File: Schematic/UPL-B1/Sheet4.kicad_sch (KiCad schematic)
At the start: 60 parts

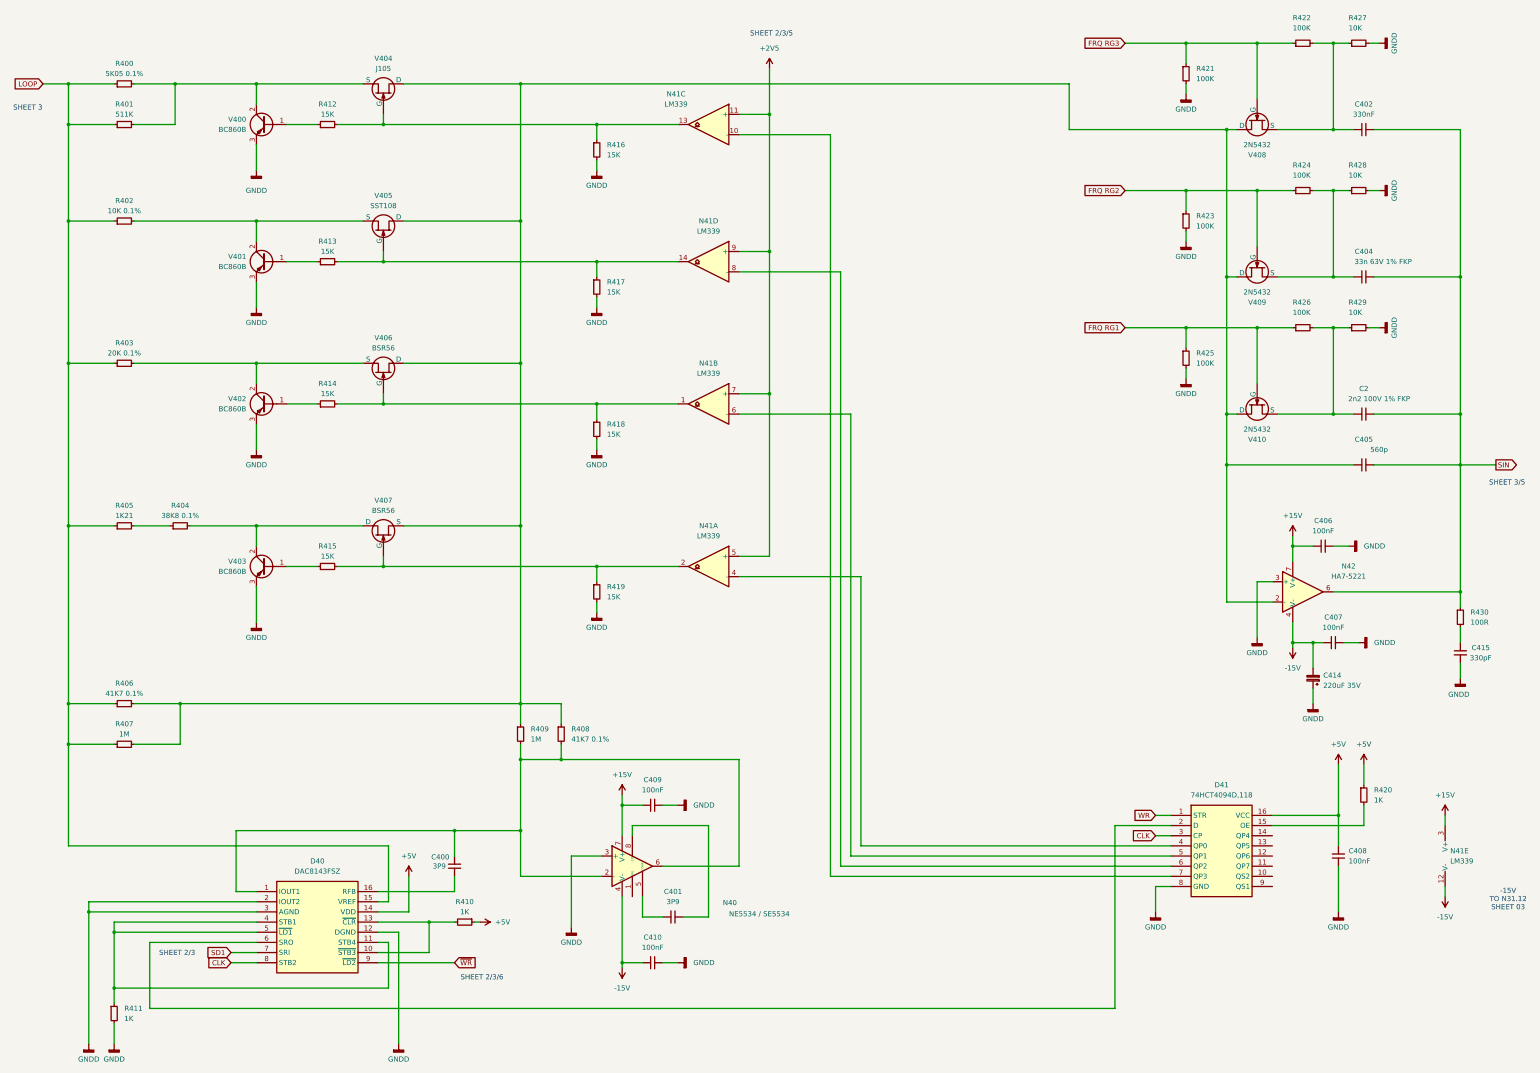
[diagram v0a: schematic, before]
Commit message: Added Integrator 1 and Level control
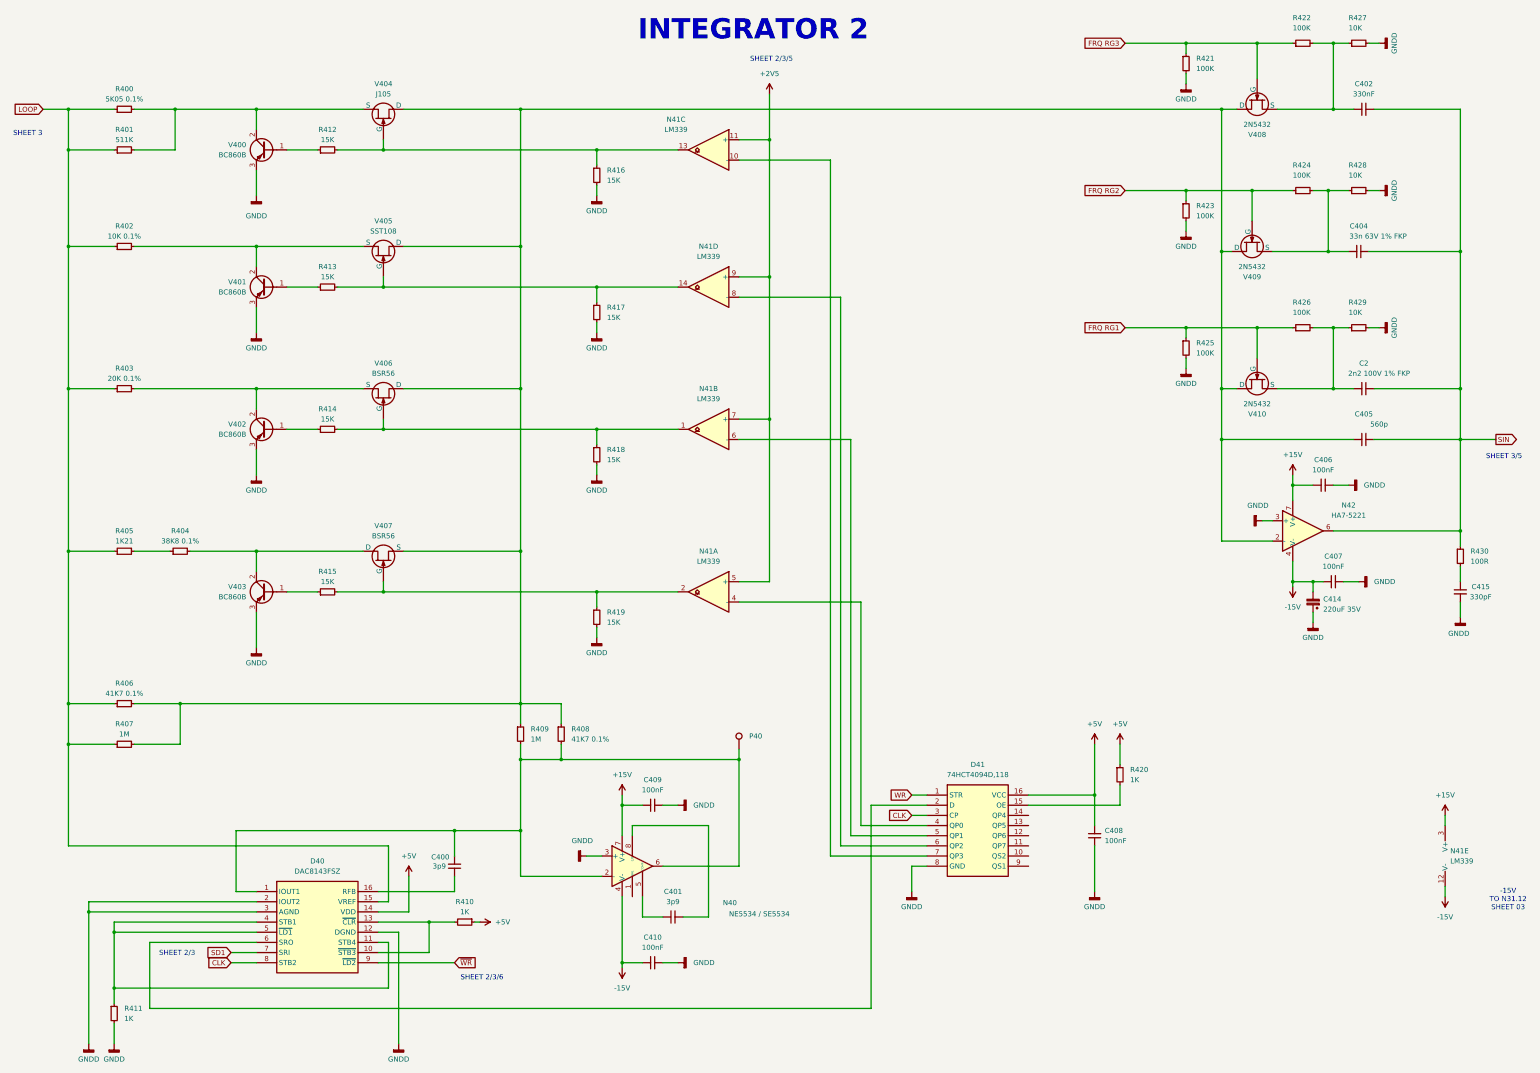
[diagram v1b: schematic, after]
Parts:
- added P40: TestPoint, symbol Connector:TestPoint
- C400, C401: value 3P9 -> 3p9
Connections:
- net at C400.2, D40.1 (IOUT1), N40.2 (-)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: now also P40.1
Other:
- note added: "INTEGRATOR 2"
- moved on the sheet: C2, C402, C404, C405, C406, C407, C408, C414, C415, D41, N41A, N41B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

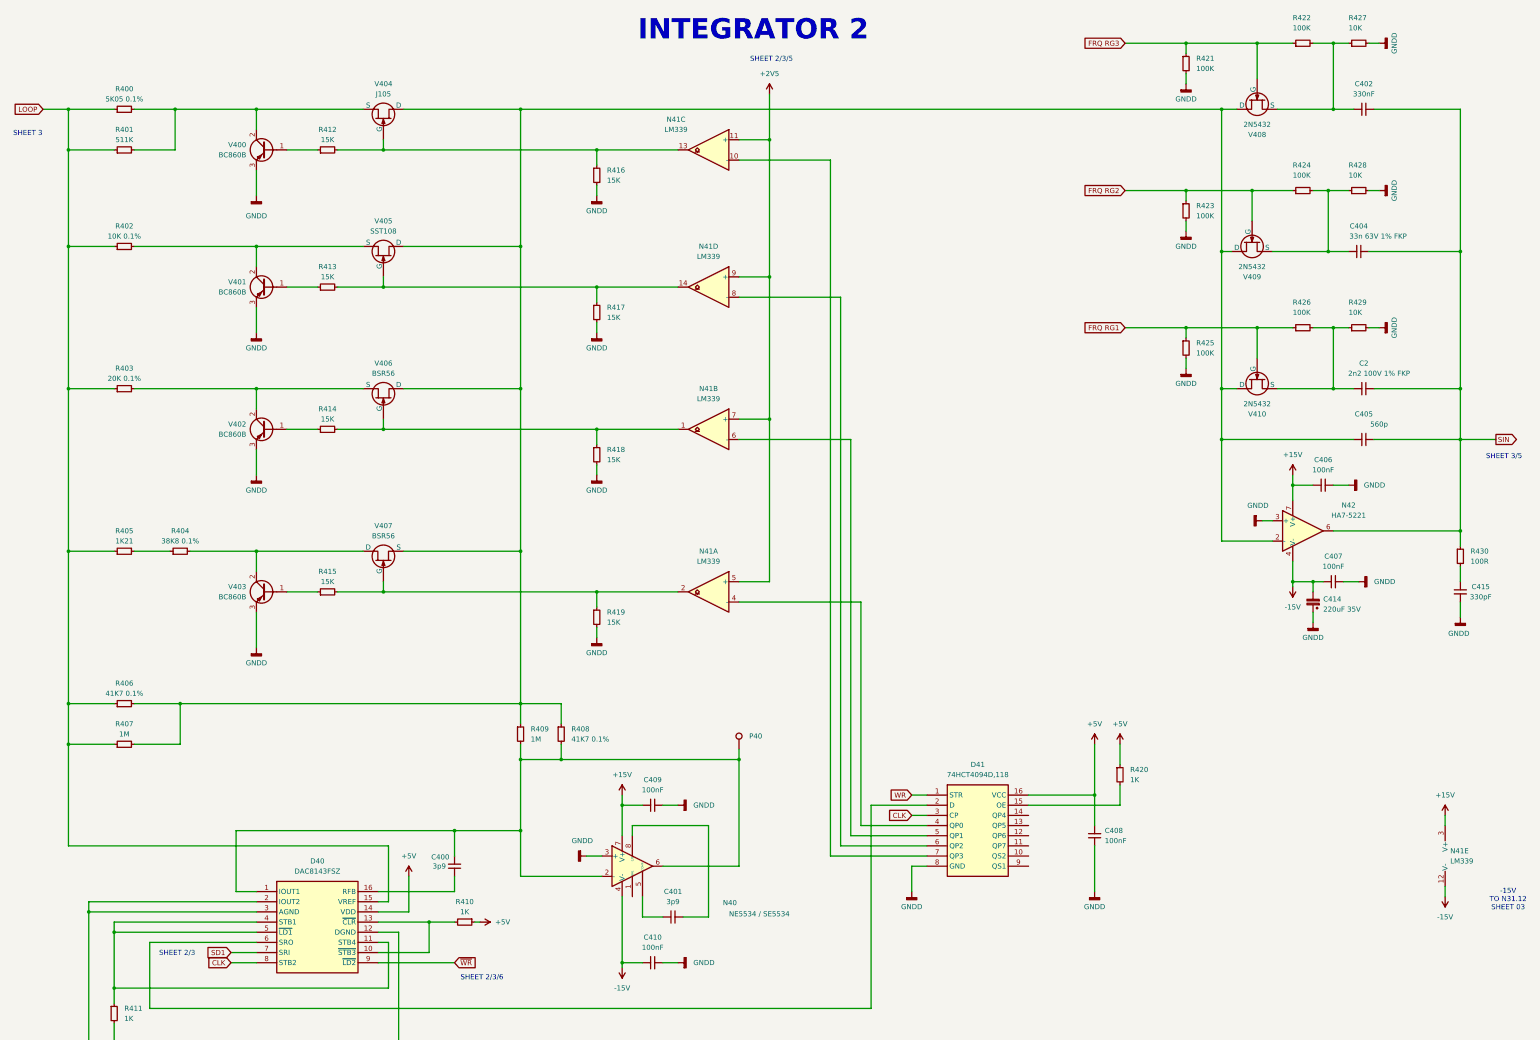
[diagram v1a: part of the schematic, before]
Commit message: Add device datasheets, begin migration to hierarchical labels
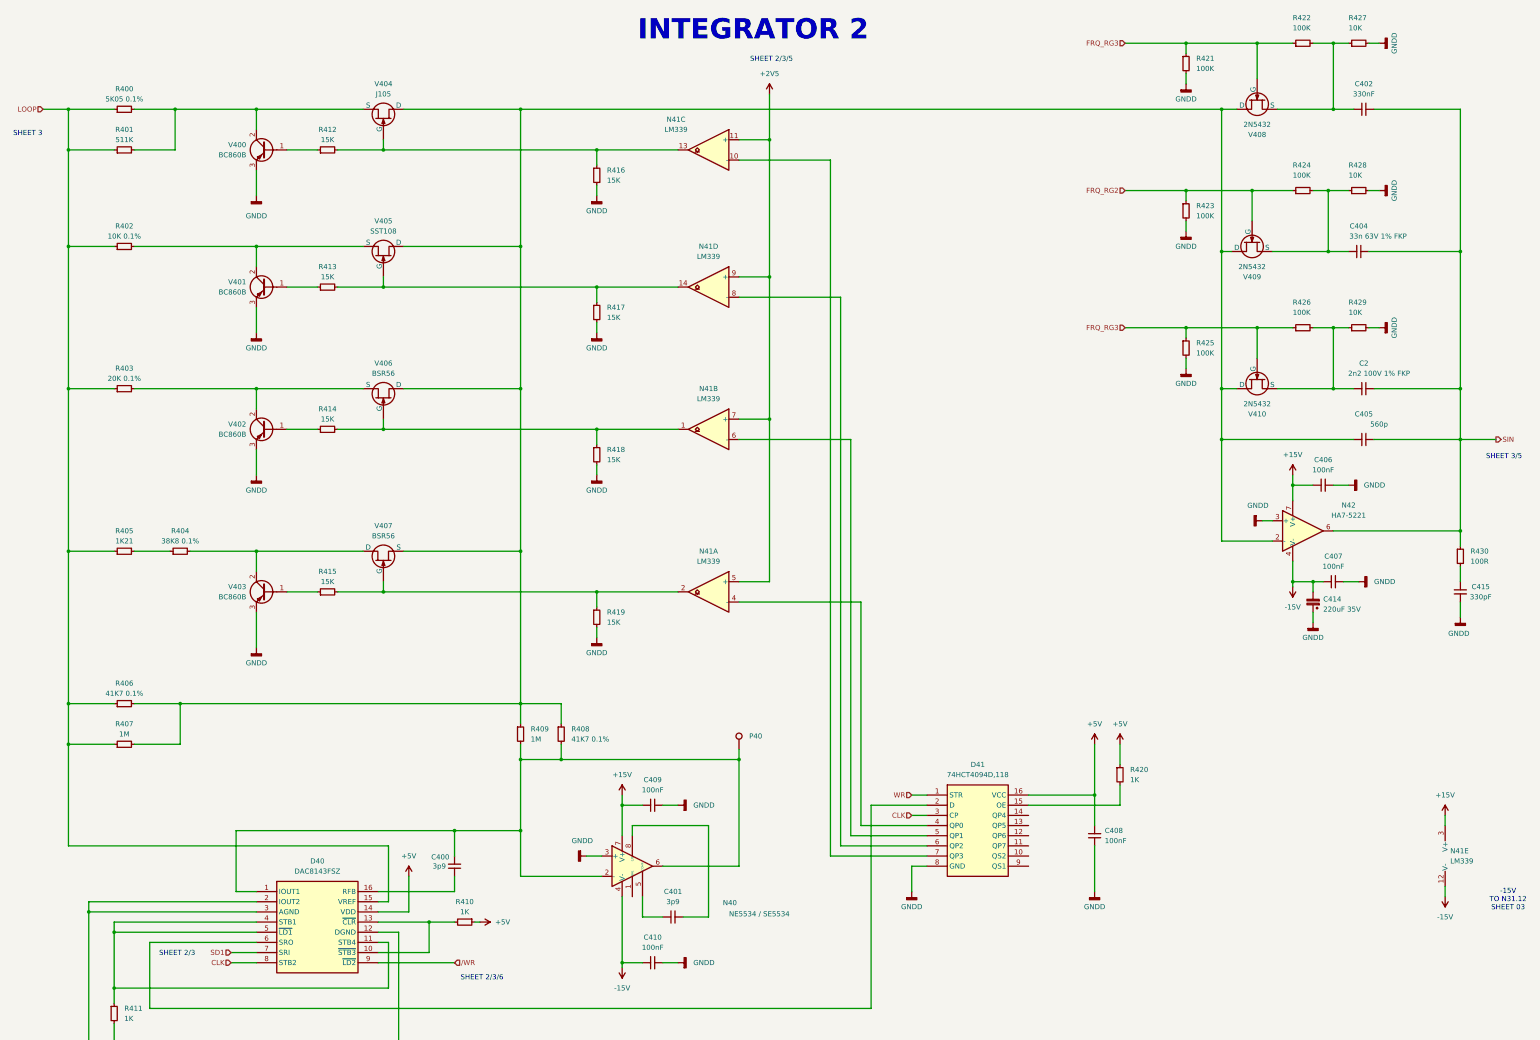
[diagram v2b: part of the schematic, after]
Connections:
- net FRQ RG3 is gone; now on net FRQ_RG3: R421.1, R422.1, V408.2 (G)
- net FRQ RG1 renamed FRQ_RG3
- net FRQ RG2 renamed FRQ_RG2
- net ~{WR} renamed /WR
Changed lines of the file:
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@@
 		)
 	)
-	(global_label "SIN"
-		(shape output)
-		(at 388.62 121.92 0)
-		(fields_autoplaced yes)
+	(hierarchical_label "CLK"
+		(shape input)
+		(at 72.39 252.73 180)
 		(effects
 			(font
 				(size 1.27 1.27)
 			)
-			(justify left)
-		)
-		(property "Intersheetrefs" "${INTERSHEET_REFS}"
-			(at 394.75 121.92 0)
-			(effects
-				(font
-					(size 1.27 1.27)
-				)
-				(justify left)
-				(hide yes)
-			)
+			(justify right)
 		)
 	)
-	(global_label "FRQ RG1"
+	(hierarchical_label "WR"
 		(shape input)
-		(at 295.91 93.98 180)
-		(fields_autoplaced yes)
+		(at 242.57 210.82 180)
 		(effects
 			(font
@@
 			(justify right)
 		)
-		(property "Intersheetrefs" "${INTERSHEET_REFS}"
-			(at 284.5186 93.98 0)
-			(effects
-				(font
-					(size 1.27 1.27)
-				)
-				(justify right)
-				(hide yes)
-			)
-		)
 	)
-	(global_label "~{WR}"
+	(hierarchical_label "{slash}WR"
 		(shape input)
 		(at 128.27 252.73 0)
-		(fields_autoplaced yes)
 		(effects
 			(font
@@
 			(justify left)
 		)
-		(property "Intersheetrefs" "${INTERSHEET_REFS}"
-			(at 133.9766 252.73 0)
-			(effects
-				(font
-					(size 1.27 1.27)
-				)
-				(justify left)
-				(hide yes)
-			)
-		)
 	)
-	(global_label "WR"
+	(hierarchical_label "LOOP"
 		(shape input)
-		(at 242.57 210.82 180)
-		(fields_autoplaced yes)
+		(at 25.4 39.37 180)
 		(effects
 			(font
@@
 			(justify right)
 		)
-		(property "Intersheetrefs" "${INTERSHEET_REFS}"
-			(at 236.8634 210.82 0)
-			(effects
-				(font
-					(size 1.27 1.27)
-				)
-				(justify right)
-				(hide yes)
-			)
-		)
 	)
-	(global_label "FRQ RG2"
-		(shape input)
-		(at 295.91 59.69 180)
-		(fields_autoplaced yes)
+	(hierarchical_label "SIN"
+		(shape output)
+		(at 388.62 121.92 0)
 		(effects
 			(font
 				(size 1.27 1.27)
 			)
-			(justify right)
-		)
-		(property "Intersheetrefs" "${INTERSHEET_REFS}"
-			(at 284.5186 59.69 0)
-			(effects
-				(font
-					(size 1.27 1.27)
-				)
-				(justify right)
-				(hide yes)
-			)
+			(justify left)
 		)
 	)
-	(global_label "CLK"
+	(hierarchical_label "FRQ_RG3"
 		(shape input)
-		(at 72.39 252.73 180)
-		(fields_autoplaced yes)
+		(at 295.91 93.98 180)
 		(effects
 			(font
@@
 			(justify right)
 		)
-		(property "Intersheetrefs" "${INTERSHEET_REFS}"
-			(at 65.8367 252.73 0)
-			(effects
-				(font
-					(size 1.27 1.27)
-				)
-				(justify right)
-				(hide yes)
-			)
-		)
 	)
-	(global_label "CLK"
+	(hierarchical_label "FRQ_RG3"
 		(shape input)
-		(at 242.57 215.9 180)
-		(fields_autoplaced yes)
+		(at 295.91 22.86 180)
 		(effects
 			(font
@@
 			(justify right)
 		)
-		(property "Intersheetrefs" "${INTERSHEET_REFS}"
-			(at 236.0167 215.9 0)
-			(effects
-				(font
-					(size 1.27 1.27)
-				)
-				(justify right)
-				(hide yes)
-			)
-		)
 	)
-	(global_label "SD1"
+	(hierarchical_label "FRQ_RG2"
 		(shape input)
-		(at 72.39 250.19 180)
-		(fields_autoplaced yes)
+		(at 295.91 59.69 180)
 		(effects
 			(font
@@
 			(justify right)
 		)
-		(property "Intersheetrefs" "${INTERSHEET_REFS}"
-			(at 65.7158 250.19 0)
-			(effects
-				(font
-					(size 1.27 1.27)
-				)
-				(justify right)
-				(hide yes)
-			)
-		)
 	)
-	(global_label "LOOP"
+	(hierarchical_label "SD1"
 		(shape input)
-		(at 25.4 39.37 180)
-		(fields_autoplaced yes)
+		(at 72.39 250.19 180)
 		(effects
 			(font
@@
 			(justify right)
 		)
-		(property "Intersheetrefs" "${INTERSHEET_REFS}"
-			(at 17.4557 39.37 0)
-			(effects
-				(font
-					(size 1.27 1.27)
-				)
-				(justify right)
-				(hide yes)
-			)
-		)
 	)
-	(global_label "FRQ RG3"
+	(hierarchical_label "CLK"
 		(shape input)
-		(at 295.91 22.86 180)
-		(fields_autoplaced yes)
+		(at 242.57 215.9 180)
 		(effects
 			(font
@@
 			(justify right)
 		)
-		(property "Intersheetrefs" "${INTERSHEET_REFS}"
-			(at 284.5186 22.86 0)
-			(effects
-				(font
-					(size 1.27 1.27)
-				)
-				(justify right)
-				(hide yes)
-			)
-		)
 	)
 	(symbol
@@
 			)
 		)
-		(property "Datasheet" "https://ngspice.sourceforge.io/docs/ngspice-html-manual/manual.xhtml#cha_JFETs"
+		(property "Datasheet" "https://www.nxp.com/docs/en/data-sheet/BSR56_57_58.pdf"
 			(at 110.49 152.4 0)
 			(effects
@@
 			)
 		)
-		(property "Datasheet" "~"
+		(property "Datasheet" "https://assets.nexperia.com/documents/data-sheet/BC859_BC860.pdf"
 			(at 81.28 49.53 0)
 			(effects
@@
 			)
 		)
-		(property "Datasheet" "~"
+		(property "Datasheet" "https://assets.nexperia.com/documents/data-sheet/BC859_BC860.pdf"
 			(at 81.28 160.02 0)
 			(effects
@@
 			)
 		)
-		(property "Datasheet" "~"
+		(property "Datasheet" "https://assets.nexperia.com/documents/data-sheet/BC859_BC860.pdf"
 			(at 81.28 83.82 0)
 			(effects
@@
 			)
 		)
-		(property "Datasheet" "https://ngspice.sourceforge.io/docs/ngspice-html-manual/manual.xhtml#cha_JFETs"
+		(property "Datasheet" "https://mm.digikey.com/Volume0/opasdata/d220001/medias/docus/906/J105%2C6%2C7.pdf"
 			(at 110.49 41.91 0)
 			(effects
@@
 			)
 		)
-		(property "Datasheet" "~"
+		(property "Datasheet" "https://assets.nexperia.com/documents/data-sheet/BC859_BC860.pdf"
 			(at 81.28 119.38 0)
 			(effects
@@
 			)
 		)
-		(property "Datasheet" "https://ngspice.sourceforge.io/docs/ngspice-html-manual/manual.xhtml#cha_JFETs"
+		(property "Datasheet" "https://www.nxp.com/docs/en/data-sheet/BSR56_57_58.pdf"
 			(at 110.49 111.76 0)
 			(effects
